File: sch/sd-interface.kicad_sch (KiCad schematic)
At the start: 34 parts, among them J15 F32Q-1A7H1-11022, J16 MEM2075-00-140-01-A, J17 3V5_out, Q1 Q_PMOS_GSD, U10 CD4043BDR, U11 TPS22919DCKR, U8 MAX4996LETG_, U9 SN74AVCH4T245PW

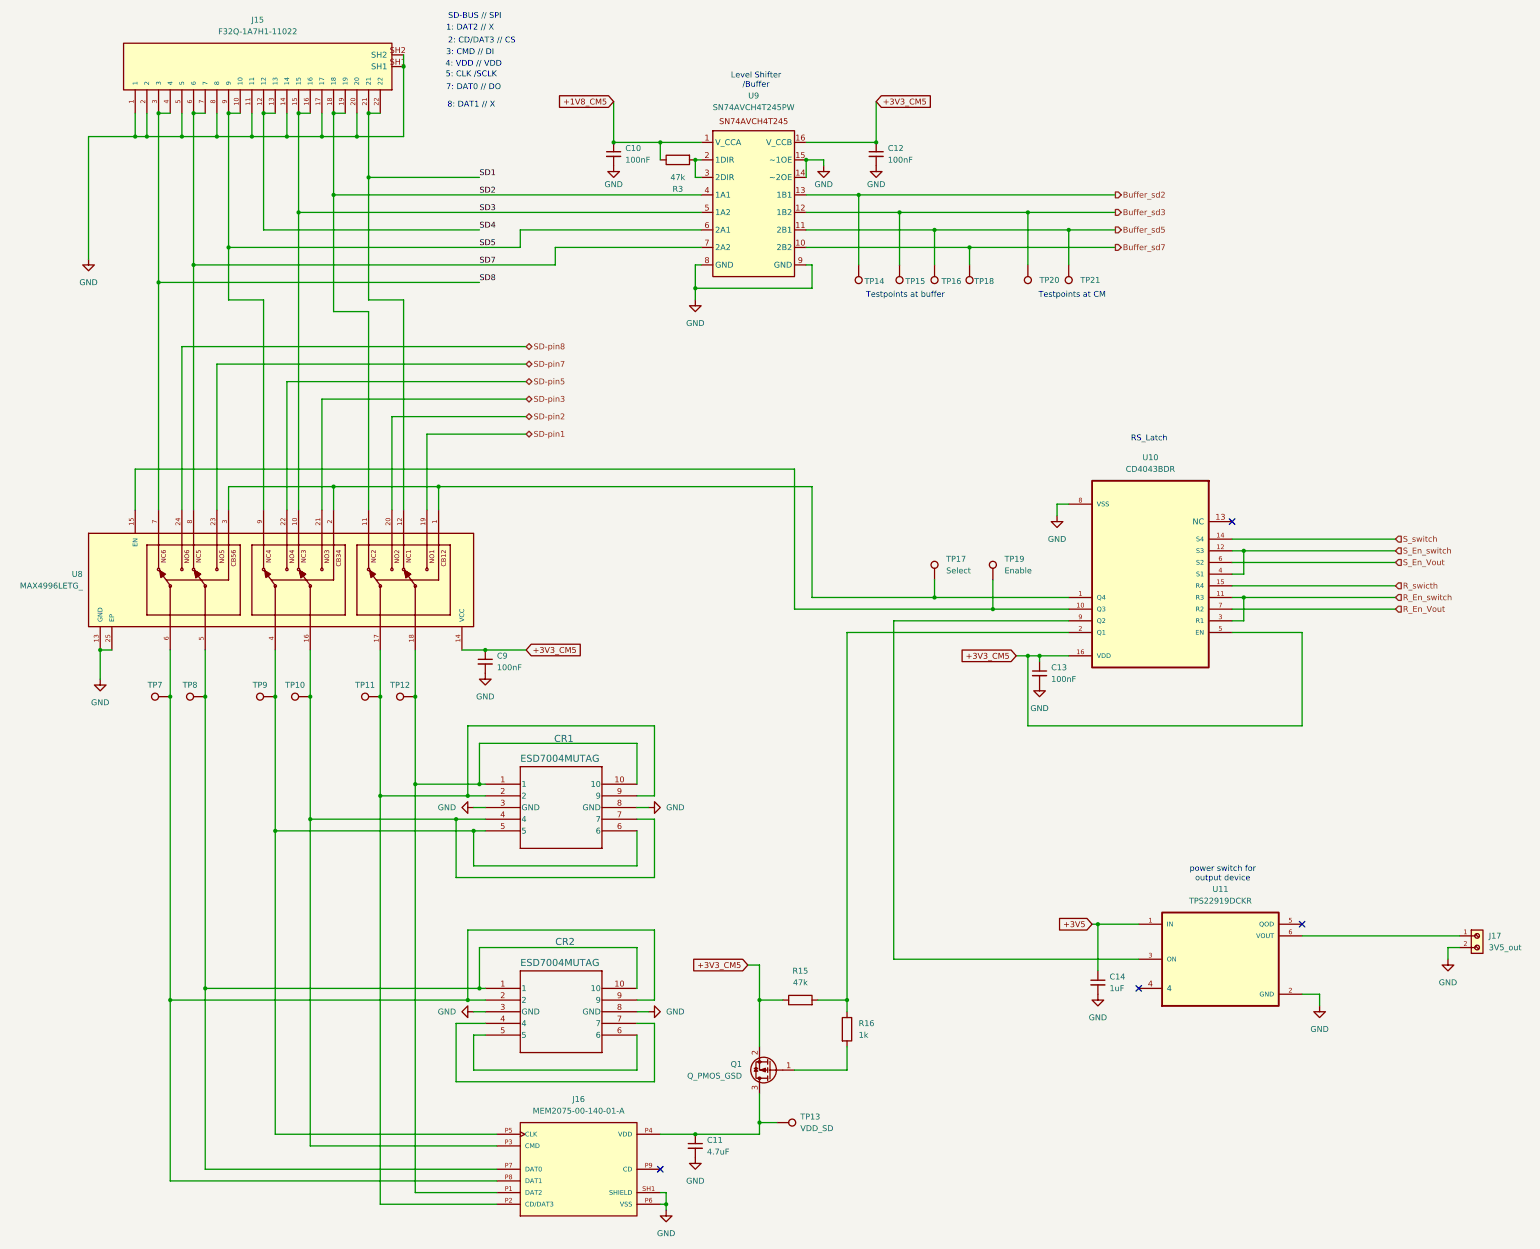
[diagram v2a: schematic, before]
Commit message: changed sd lines impedanc etc. power plane zone 3.3v
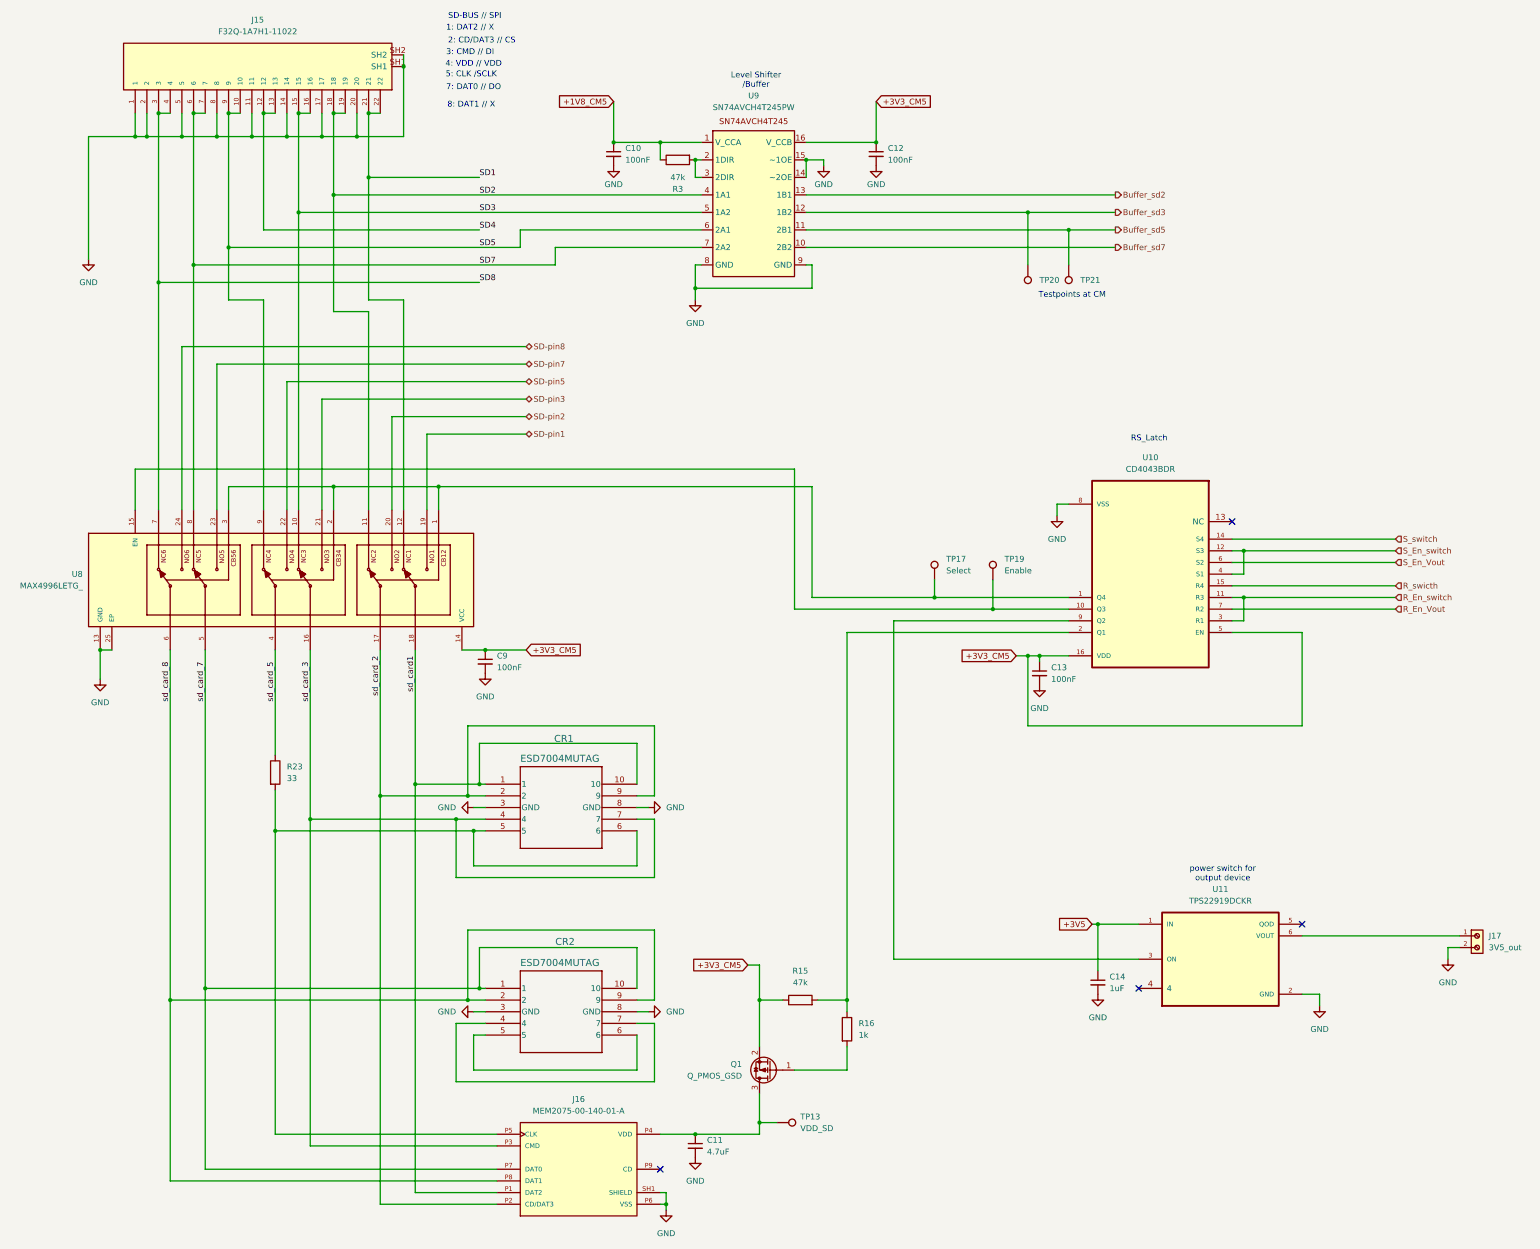
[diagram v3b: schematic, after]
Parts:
- removed TP10, TP11, TP12, TP7, TP8, TP9: TestPoint, TestPoint:TestPoint_Pad_D1.0mm, symbol Connector:TestPoint
- removed TP14, TP15, TP16, TP18: TestPoint, TestPoint:TestPoint_Loop_D2.60mm_Drill1.6mm_Beaded, symbol Connector:TestPoint
- added R23: 33, Resistor_SMD:R_0402_1005Metric, symbol Device:R
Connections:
- net sd_card_7: now reaches CR2.1, CR2.10, J16.P7 (DAT0), U8.5
- net sd_card_8: now reaches CR2.2, CR2.9, J16.P8 (DAT1), U8.6
- net sd_card1: now reaches CR1.1, CR1.10, J16.P1 (DAT2), U8.18
- net sd_card_2: now reaches CR1.2, CR1.9, J16.P2 (CD/DAT3), U8.17
- net sd_card_3: now reaches CR1.4, CR1.7, J16.P3 (CMD), U8.16
- net at CR1.5, CR1.6, J16.P5 (CLK): now also R23.2; no longer U8.4
- new net sd_card_5: R23.1, U8.4
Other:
- note removed: "Testpoints at buffer"

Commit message: update licence to CERN-OHL-S
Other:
- title: (none) -> Audiograb

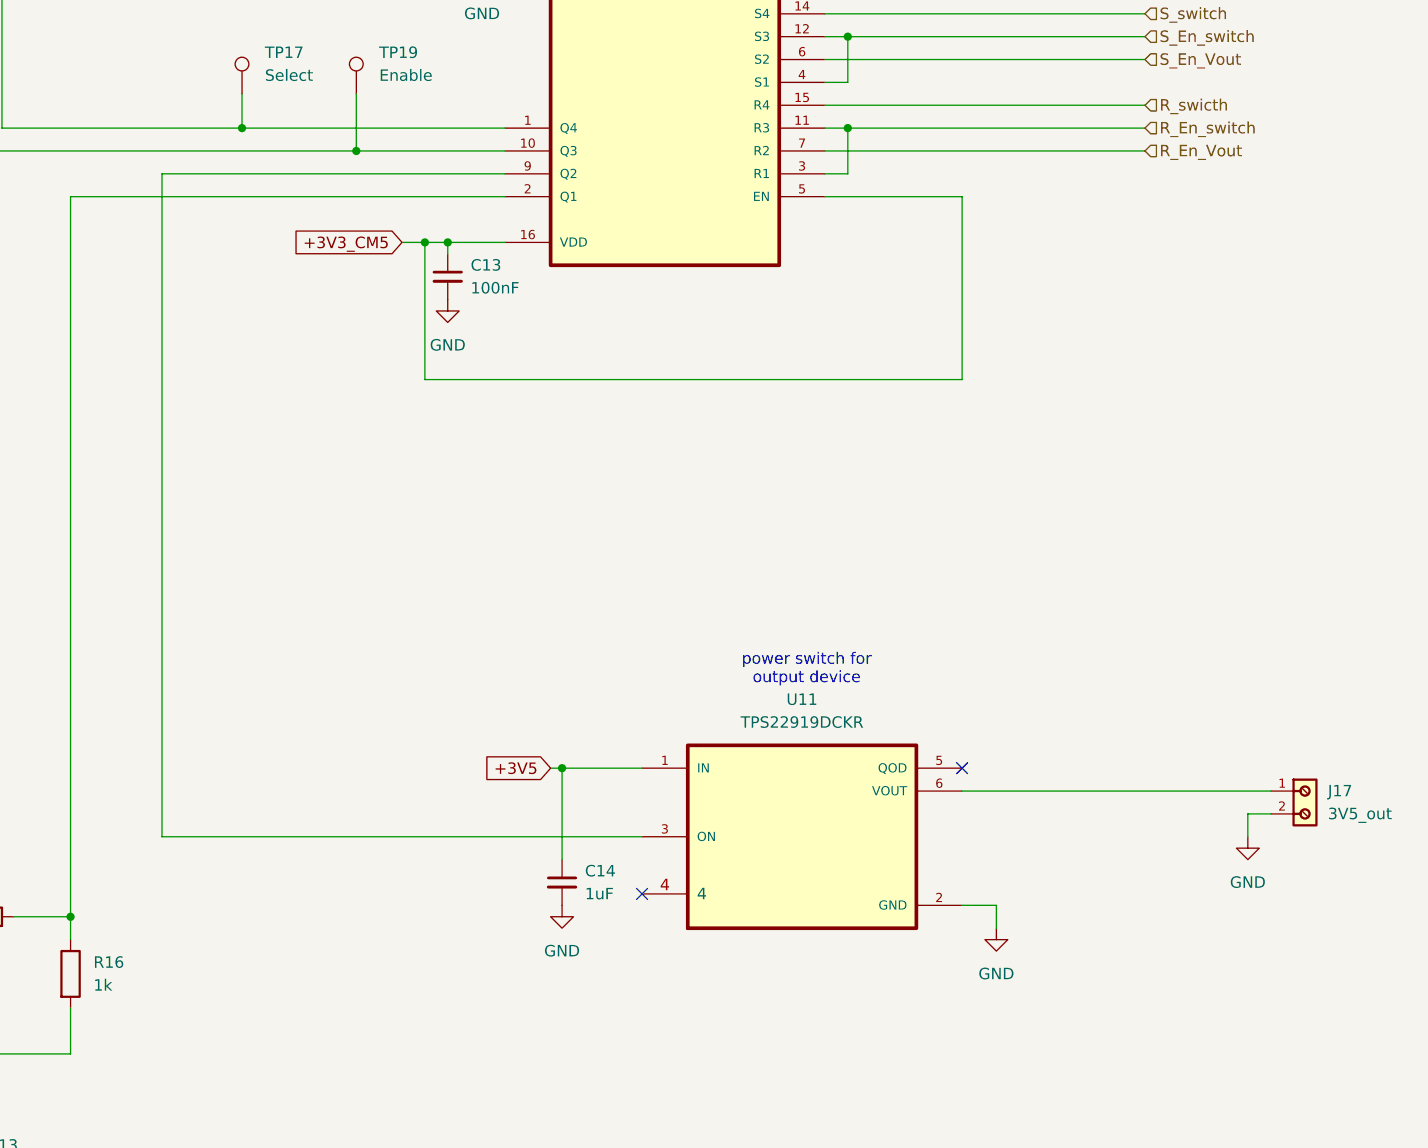
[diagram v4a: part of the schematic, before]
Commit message: Ryddet i schematic og satt inn 3D figurer
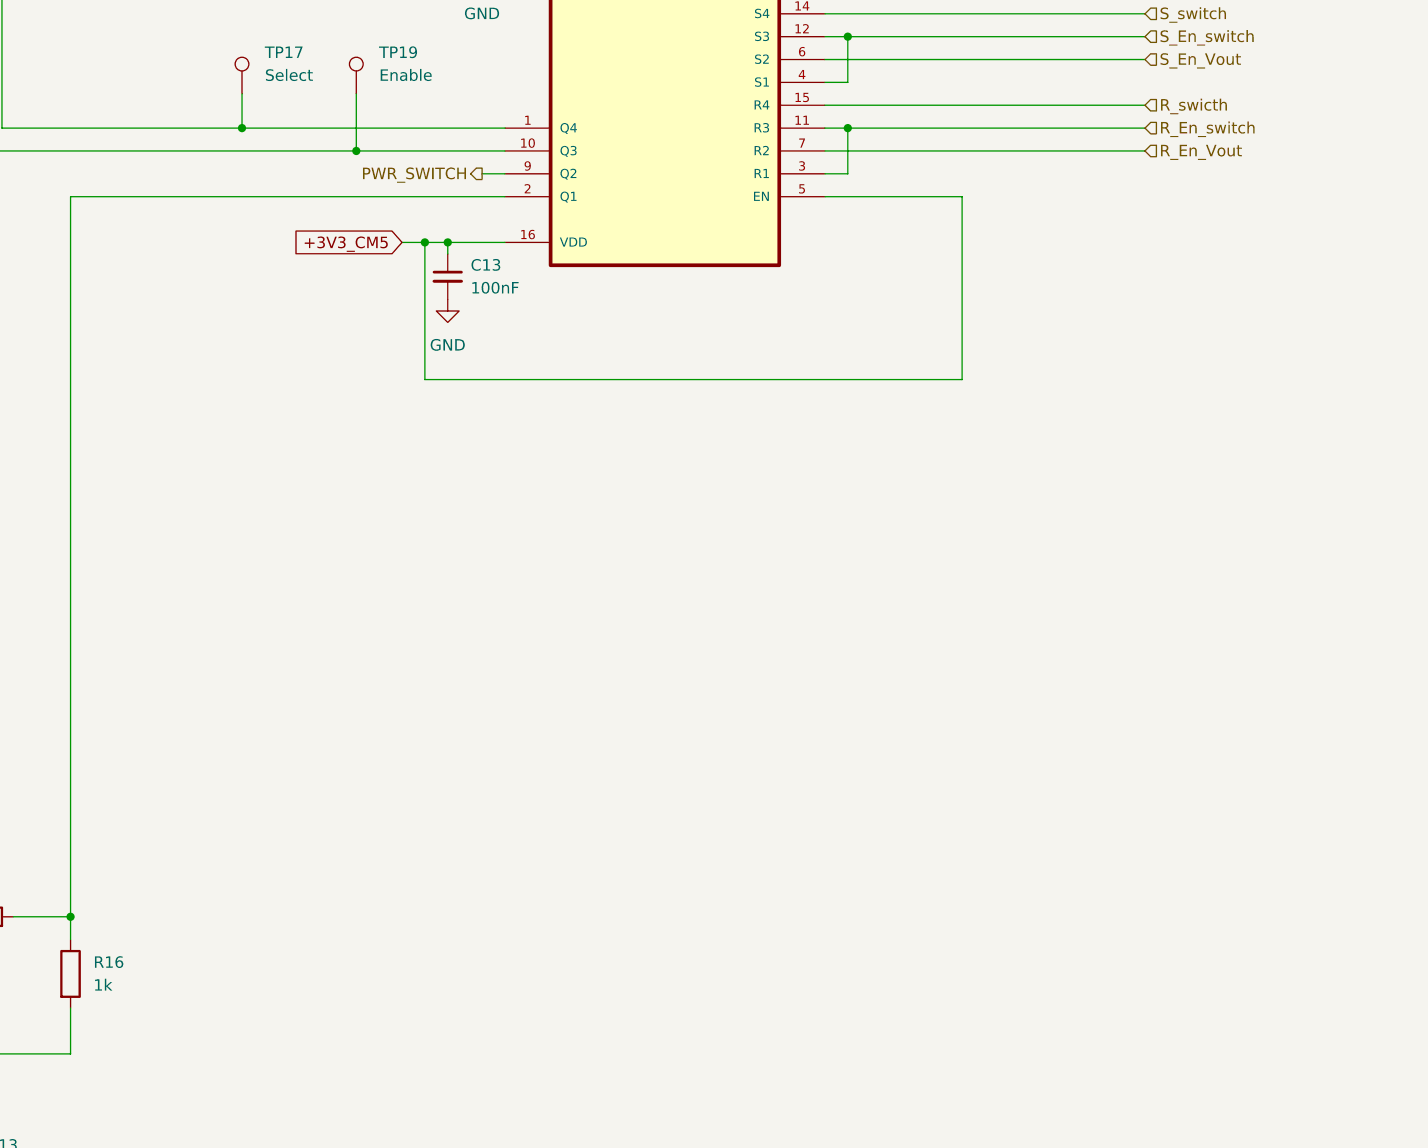
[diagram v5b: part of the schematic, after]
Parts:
- removed C14: 1uF, Capacitor_SMD:C_0603_1608Metric, symbol Device:C_Small
- removed J17: 3V5_out, 691137710002:691137710002, symbol 691137710002:691137710002
- removed U11: TPS22919DCKR, TPS22919DCKR:SOT65P210X110-6N, symbol TPS22919DCKR:TPS22919DCKR
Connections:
- net PWR_SWITCH: now reaches U10.9 (Q2)
- no-connect marks 4 -> 2
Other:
- note removed: "power switch for output device"
